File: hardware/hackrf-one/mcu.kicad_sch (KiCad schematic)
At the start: 131 parts, among them J1 USB-MICRO-B, P20 GPIO, P22 I2S, P23 DBGEN, P24 TRST, P25 LPC_ISP, P26 LPC_JTAG, P28 SD, P29 CPLD_JTAG, P3 GND, P30 BANK2_AUX, P5 LEDS, P68 SPIFI_CS, P69 VREGMODE, P70 EN_1V8, P71 ID, P73 P1_2, P74 P1_1, P75 GP_CLKIN, P76 GP_CLKIN, P77 GP_CLKIN, P78 GP_CLKIN, P79 GP_CLKIN, P80 SHIELD, P81 SPIFI_SIO2, P82 SPIFI_SIO3, Q5 MOSFET_P, SW1 DFU, SW2 RESET, U15 TVS, U20 W25Q80, U21 TPS62410, U23 LPC4320FBD144, U24 GSG-XC2C64A-7VQG100C, X2 MCU_XTAL, X3 RTC_XTAL

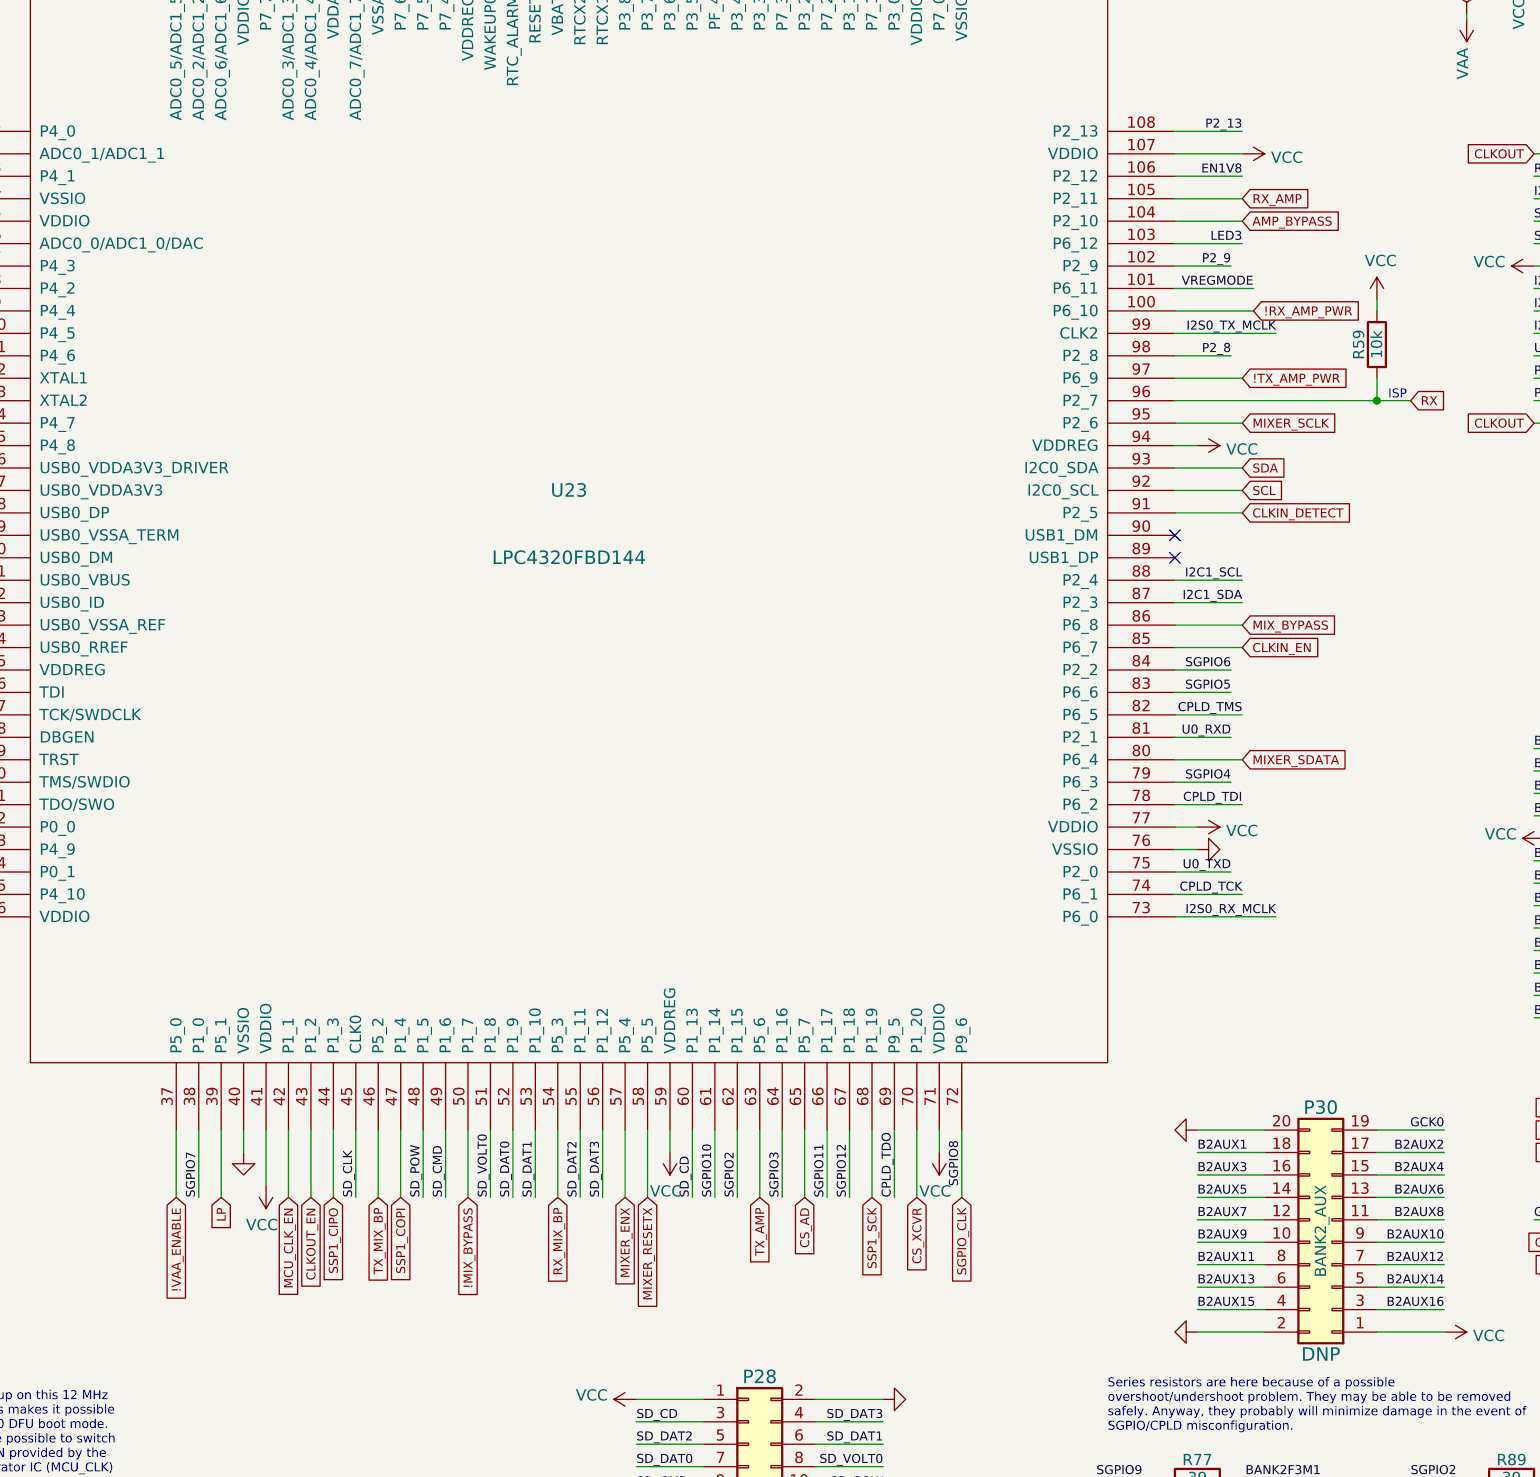
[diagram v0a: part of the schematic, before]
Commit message: HackRF One: swap pins for platform detection
- move EN_1V8 to P5_0, U23 pin 37
- move !VAA_ENABLE to P6_10, U23 pin 100
- move !RX_AMP_PWR back to P2_12, U23 pin 106

Platform detection is now performed using P5_0 and P6_10 which avoids
the complication of having to detect a pull-up to VAA which may not yet
be switched on.
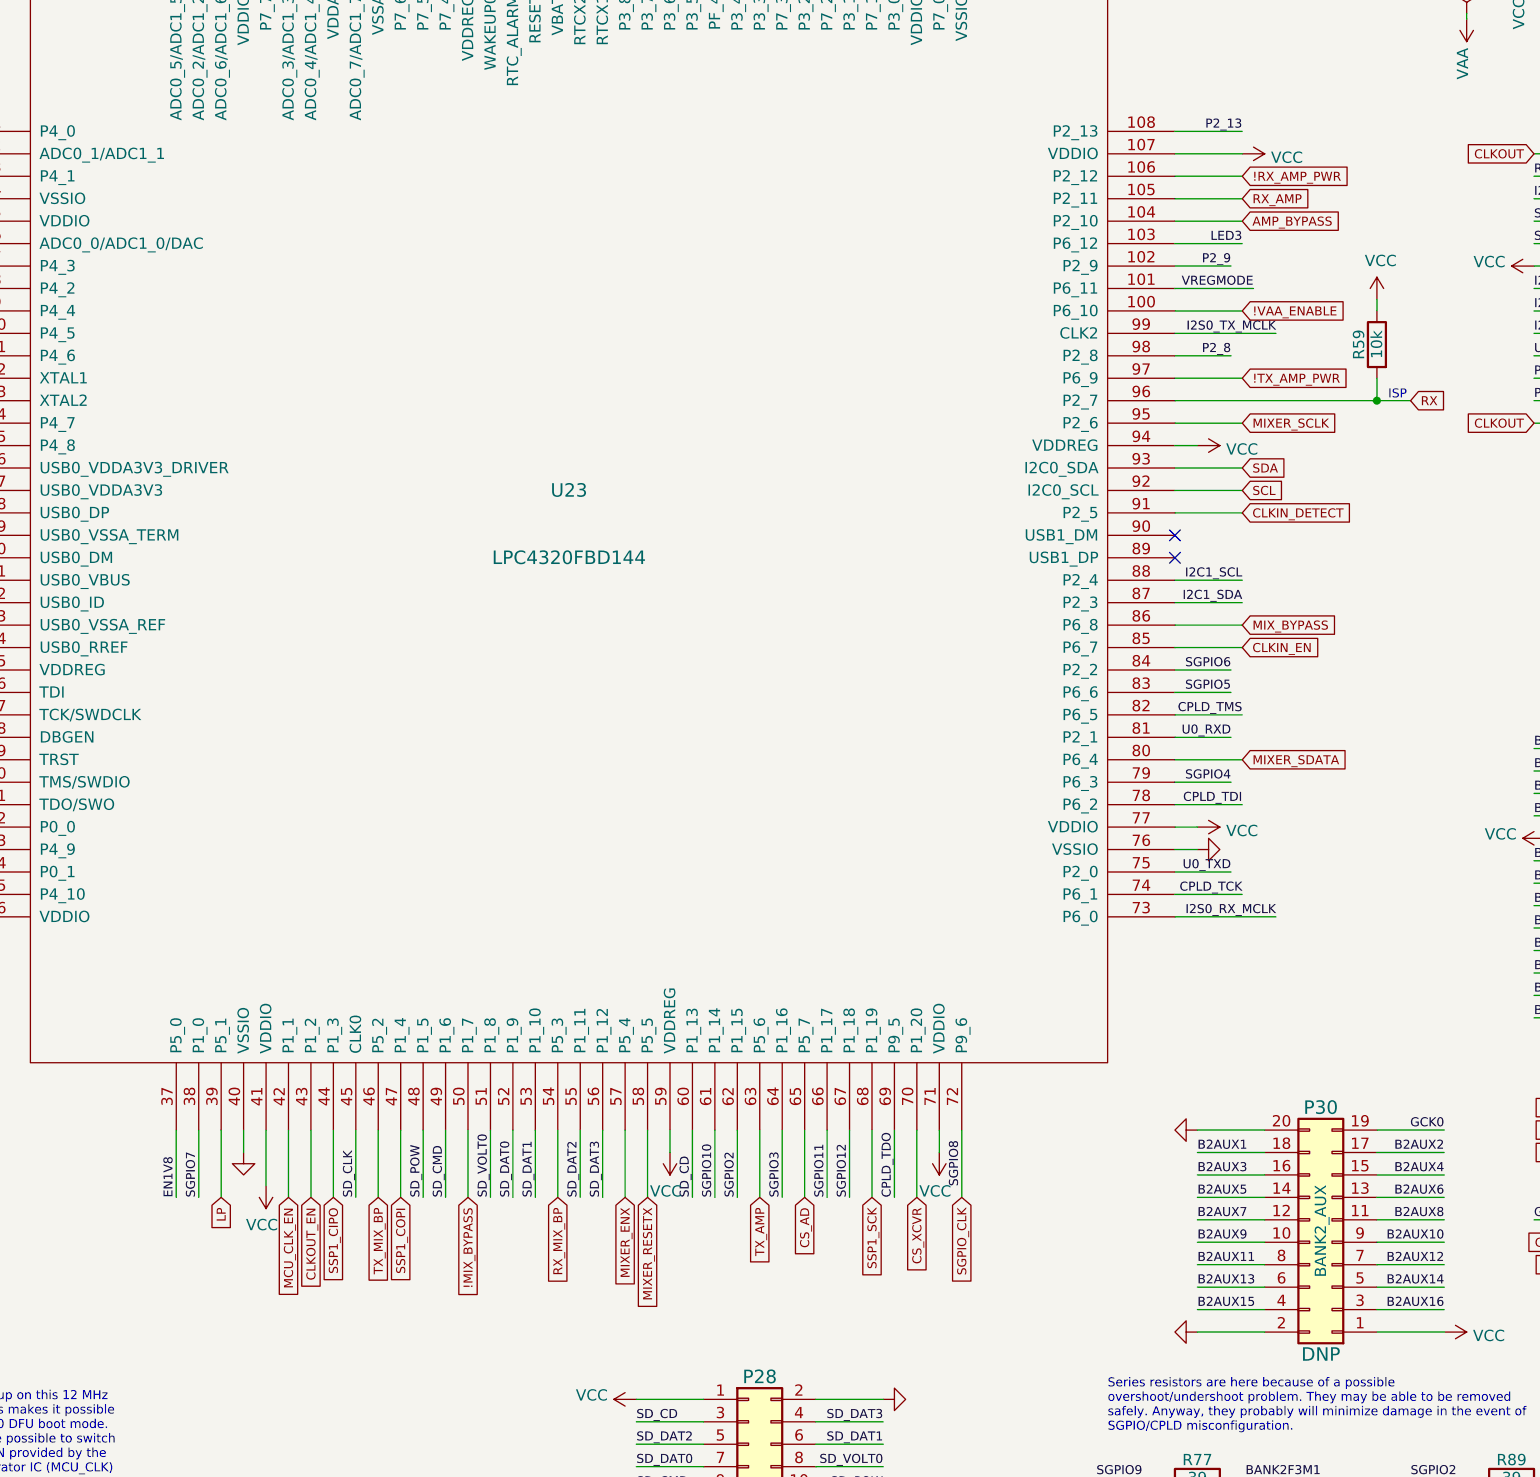
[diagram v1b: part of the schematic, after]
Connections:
- net !RX_AMP_PWR: now also U23.106 (P2_12); no longer U23.100 (P6_10)
- net !VAA_ENABLE: now also U23.100 (P6_10); no longer U23.37 (P5_0)
- net EN1V8: now also U23.37 (P5_0); no longer U23.106 (P2_12)
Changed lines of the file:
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@@
     (stroke (width 0) (type default) (color 0 0 0 0))
   )
-  (wire (pts (xy 246.38 96.52) (xy 255.27 96.52))
+  (wire (pts (xy 246.38 96.52) (xy 254 96.52))
     (stroke (width 0) (type default) (color 0 0 0 0))
   )
@@
     (effects (font (size 1.016 1.016)) (justify right bottom))
   )
-  (label "EN1V8" (at 254 81.28 180)
-    (effects (font (size 1.016 1.016)) (justify right bottom))
+  (label "EN1V8" (at 133.35 196.85 90)
+    (effects (font (size 1.016 1.016)) (justify left bottom))
   )
   (label "BANK2F3M6" (at 215.9 242.57 180)
@@
     (effects (font (size 1.016 1.016)) (justify left bottom))
   )
-  (global_label "!RX_AMP_PWR" (shape input) (at 255.27 96.52 0) (fields_autoplaced)
+  (global_label "!RX_AMP_PWR" (shape input) (at 254 81.28 0) (fields_autoplaced)
     (effects (font (size 1.016 1.016)) (justify left))
-    (property "Intersheet References" "${INTERSHEET_REFS}" (id 0) (at 1.27 15.24 0)
+    (property "Intersheet References" "${INTERSHEET_REFS}" (id 0) (at 0 0 0)
       (effects (font (size 1.27 1.27)) hide)
     )
@@
     )
   )
-  (global_label "!VAA_ENABLE" (shape input) (at 133.35 196.85 270) (fields_autoplaced)
-    (effects (font (size 1.016 1.016)) (justify right))
-    (property "Intersheet References" "${INTERSHEET_REFS}" (id 0) (at 0 0 0)
-      (effects (font (size 1.27 1.27)) hide)
-    )
+  (global_label "!VAA_ENABLE" (shape input) (at 254 96.52 0) (fields_autoplaced)
+    (effects (font (size 1.016 1.016)) (justify left))
+    (property "Intersheet References" "${INTERSHEET_REFS}" (id 0) (at 57.15 229.87 0)
+      (effects (font (size 1.27 1.27)) hide)
+    )

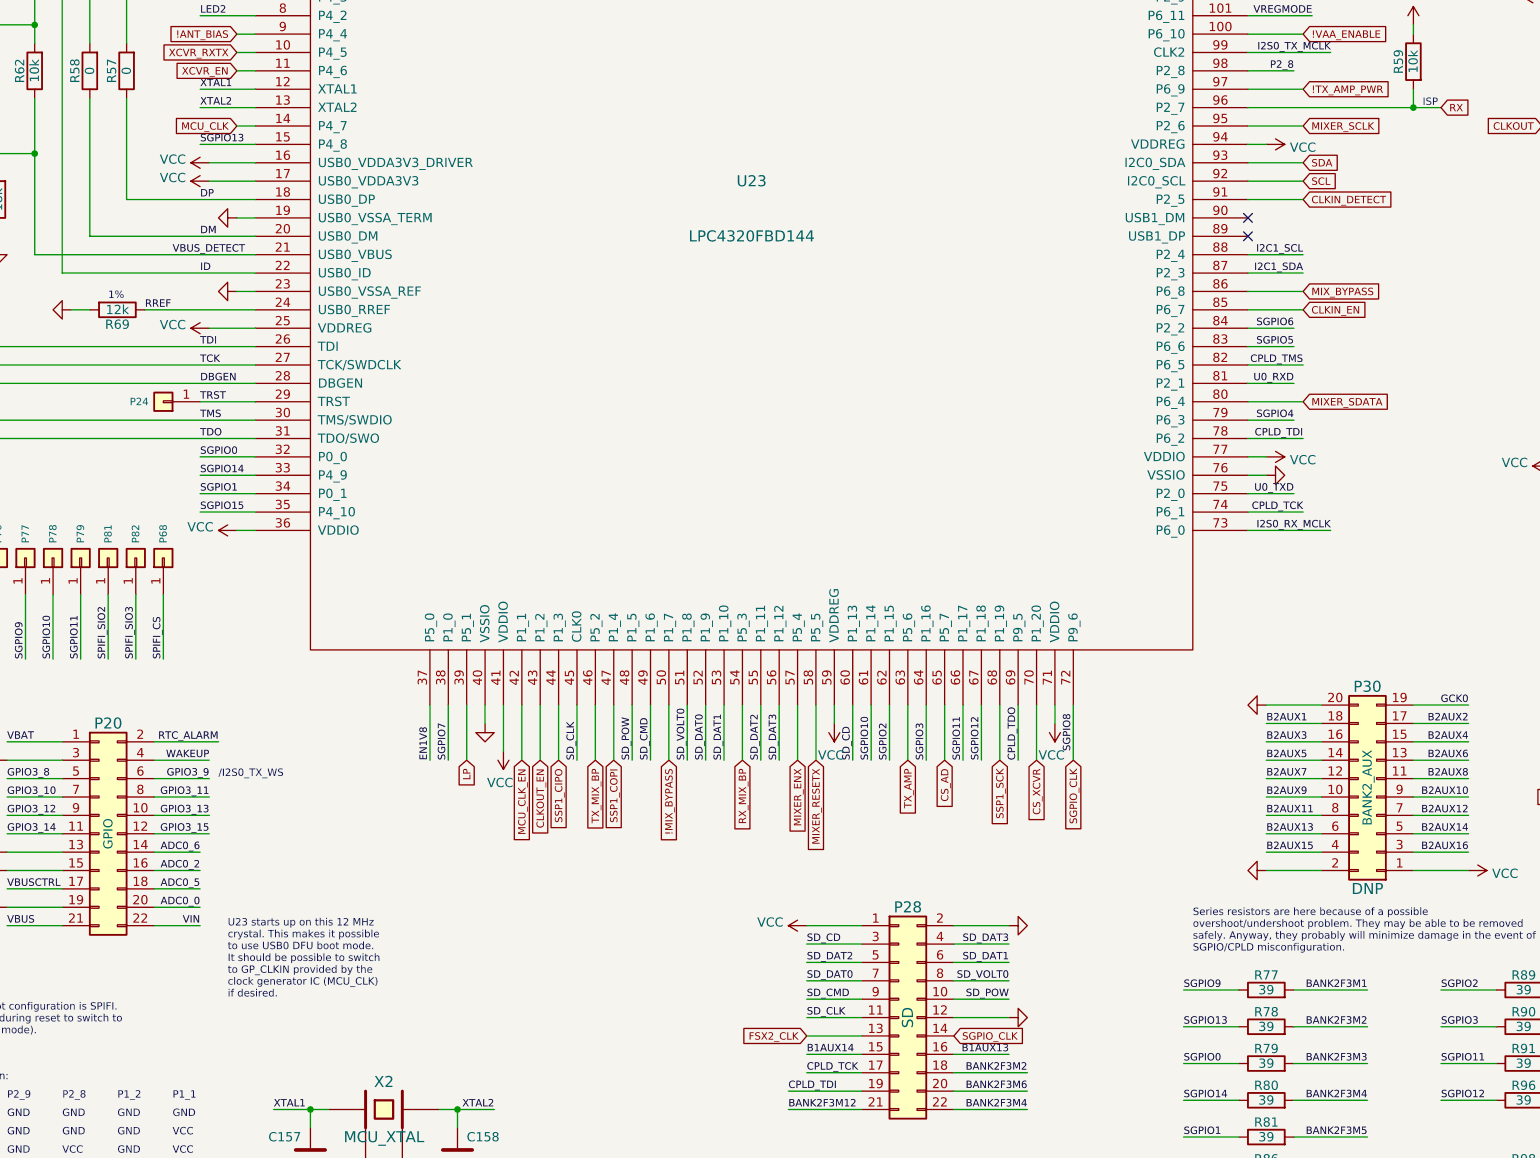
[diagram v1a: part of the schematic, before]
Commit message: HackRF One: change CLKIN_DETECT pin
- move CLKIN_DETECT to U23 pin 15, P4_8, CTIN_5
- move SGPIO13 to U23 pin 91, P2_5, GPIO5[5]
- rename SGPIO13 to TRIGGER_EN

This allows TIMER1/TIMER2 instead of TIMER3/TIMER0 to be used for CLKIN
detection, avoiding conflicts with PortaPack firmware.

SGPIO13 was never used for SGPIO, so it is renamed to reflect current
usage.
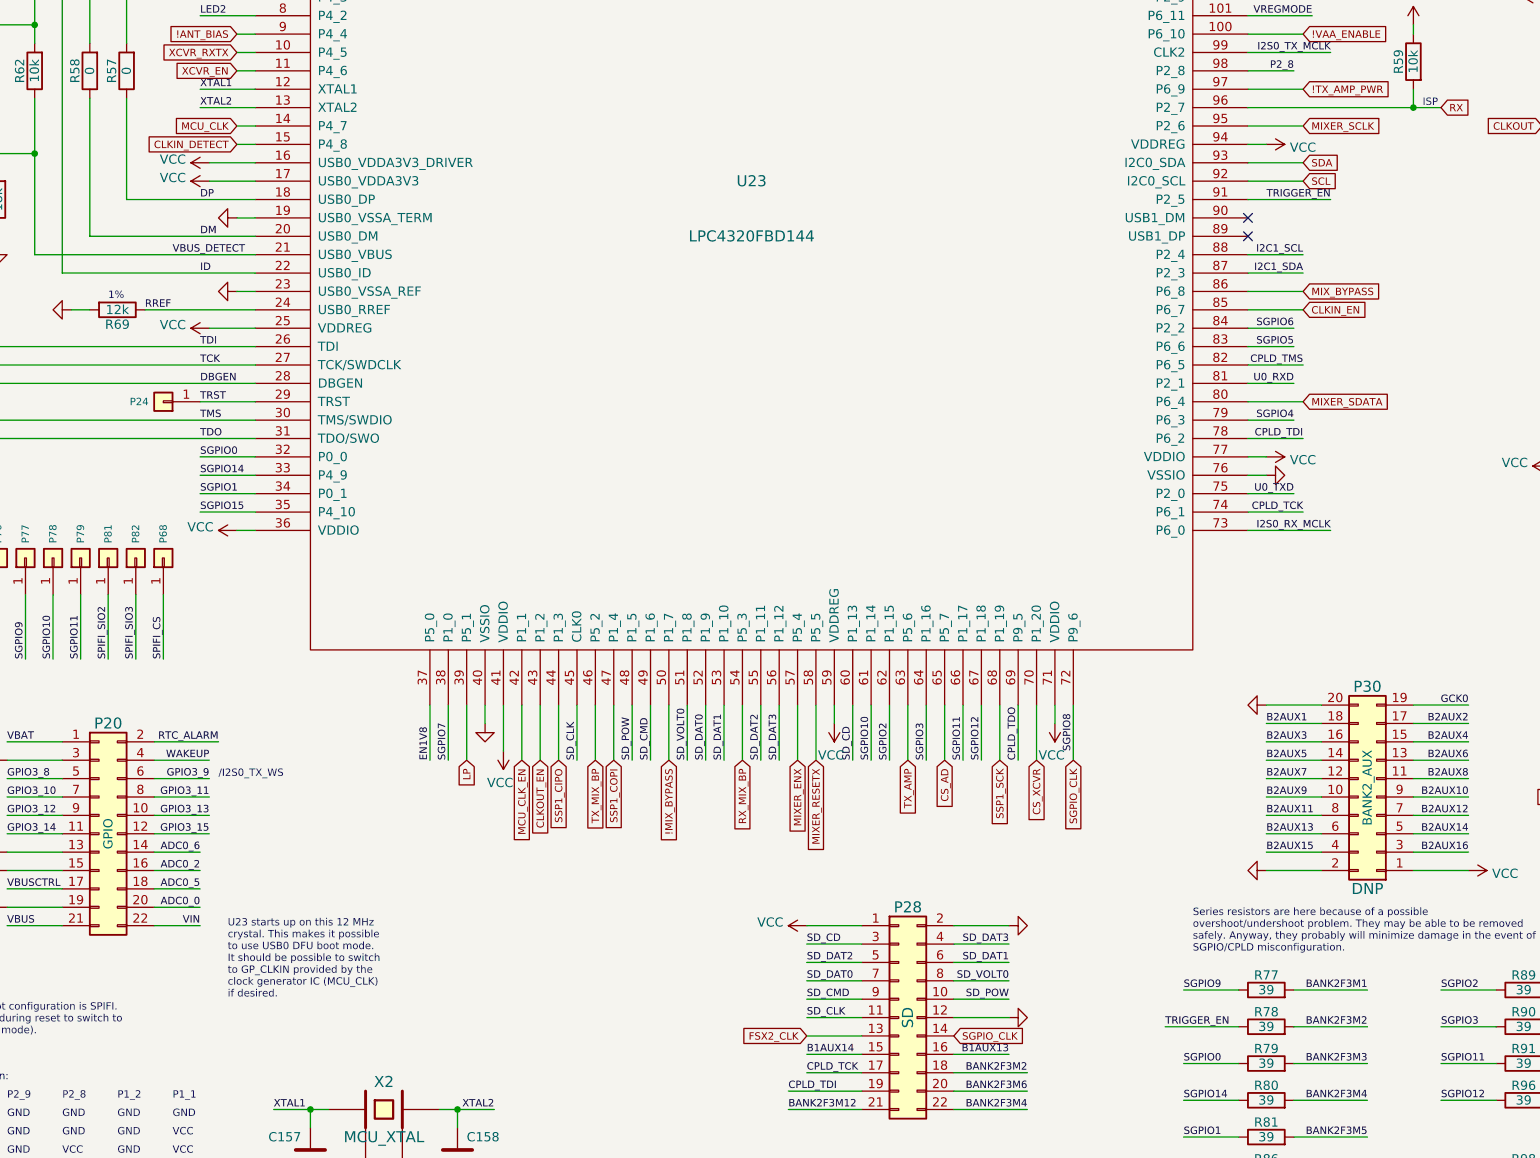
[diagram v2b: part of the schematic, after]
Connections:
- net CLKIN_DETECT: now also U23.15 (P4_8); no longer U23.91 (P2_5)
- net SGPIO13 renamed TRIGGER_EN
- net TRIGGER_EN: now also U23.91 (P2_5); no longer U23.15 (P4_8)
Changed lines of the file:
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@@
     (stroke (width 0) (type default) (color 0 0 0 0))
   )
-  (wire (pts (xy 101.6 111.76) (xy 109.22 111.76))
+  (wire (pts (xy 106.68 111.76) (xy 109.22 111.76))
     (stroke (width 0) (type default) (color 0 0 0 0))
   )
@@
     (stroke (width 0) (type default) (color 0 0 0 0))
   )
-  (wire (pts (xy 245.11 233.68) (xy 237.49 233.68))
+  (wire (pts (xy 245.11 233.68) (xy 234.95 233.68))
     (stroke (width 0) (type default) (color 0 0 0 0))
   )
@@
     (stroke (width 0) (type default) (color 0 0 0 0))
   )
-  (wire (pts (xy 254 119.38) (xy 246.38 119.38))
+  (wire (pts (xy 257.81 119.38) (xy 246.38 119.38))
     (stroke (width 0) (type default) (color 0 0 0 0))
   )
@@
     (effects (font (size 1.016 1.016)) (justify left bottom))
   )
-  (label "SGPIO13" (at 101.6 111.76 0)
-    (effects (font (size 1.016 1.016)) (justify left bottom))
+  (label "TRIGGER_EN" (at 257.81 119.38 180)
+    (effects (font (size 1.016 1.016)) (justify right bottom))
   )
   (label "VBUS" (at 304.8 66.675 90)
@@
     (effects (font (size 1.016 1.016)) (justify right bottom))
   )
-  (label "SGPIO13" (at 237.49 233.68 0)
-    (effects (font (size 1.016 1.016)) (justify left bottom))
-  )
   (label "REG_OUT2" (at 373.38 17.78 0)
     (effects (font (size 1.016 1.016)) (justify left bottom))
@@
   )
   (label "B2AUX1" (at 248.92 191.77 0)
+    (effects (font (size 1.016 1.016)) (justify left bottom))
+  )
+  (label "TRIGGER_EN" (at 234.95 233.68 0)
     (effects (font (size 1.016 1.016)) (justify left bottom))
   )
@@
     )
   )
-  (global_label "CLKIN_DETECT" (shape input) (at 254 119.38 0) (fields_autoplaced)
-    (effects (font (size 1.016 1.016)) (justify left))
-    (property "Intersheet References" "${INTERSHEET_REFS}" (id 0) (at 266.4547 119.3165 0)
-      (effects (font (size 1.016 1.016)) (justify left) hide)
-    )
-  )
+  (global_label "CLKIN_DETECT" (shape input) (at 106.68 111.76 180) (fields_autoplaced)
+    (effects (font (size 1.016 1.016)) (justify right))
+    (property "Intersheet References" "${INTERSHEET_REFS}" (id 0) (at 94.2253 111.8235 0)
+      (effects (font (size 1.016 1.016)) (justify right) hide)
+    )
+  )
